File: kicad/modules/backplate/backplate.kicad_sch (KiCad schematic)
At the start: 1 part, among them J1 10018784-10210TLF

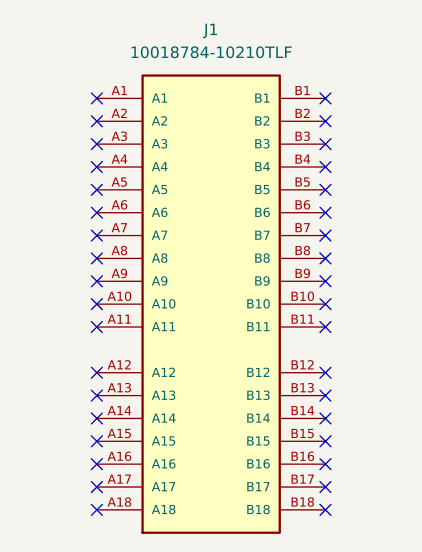
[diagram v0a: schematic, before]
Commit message: update PCIe nets
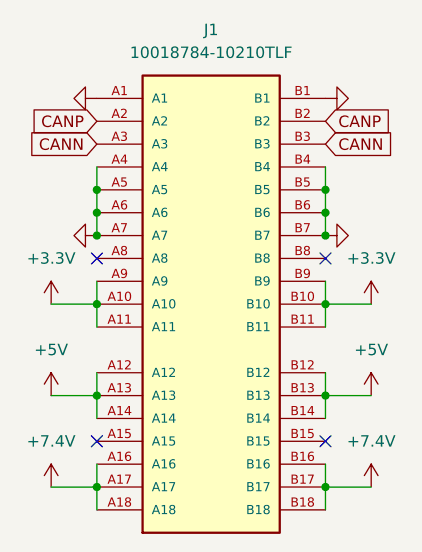
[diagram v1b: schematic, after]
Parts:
- J1: digikey # (none) -> 609-2029-ND; digikey link (none) -> https://www.digikey.ca/en/products/detail/amphenol-cs-fci/1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
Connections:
- net GND: now reaches J1.A1
- net GND: now also J1.A4, J1.A5, J1.A6, J1.A7, J1.B1, J1.B4, J1.B5, J1.B6, J1.B7
- net +3.3V: now reaches J1.A10
- net +3.3V: now also J1.A11, J1.A9, J1.B10, J1.B11, J1.B9
- net +5V: now reaches J1.A12
- net +5V: now also J1.A13, J1.A14, J1.B12, J1.B13, J1.B14
- net +7.4V: now reaches J1.A16
- net +7.4V: now also J1.A17, J1.A18, J1.B16, J1.B17, J1.B18
- net CANP: now reaches J1.A2
- net CANP: now also J1.B2
- net CANN: now reaches J1.A3
- net CANN: now also J1.B3
- no-connect marks 36 -> 4

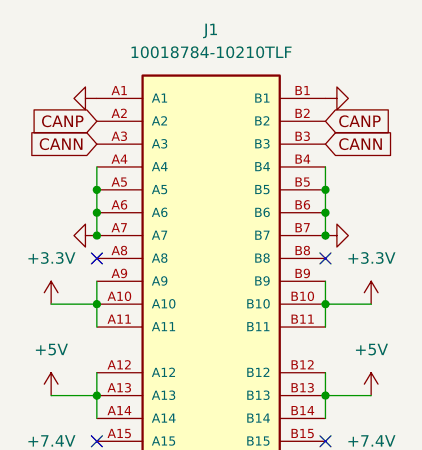
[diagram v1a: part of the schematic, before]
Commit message: backplate: update PCIe pins
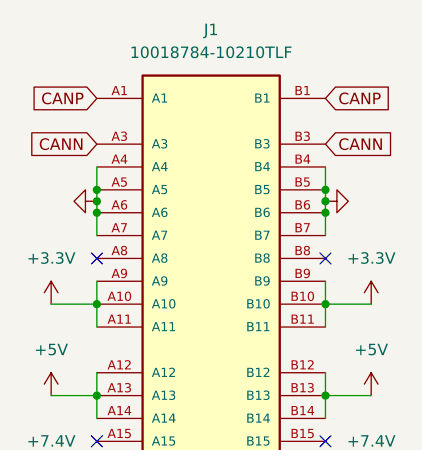
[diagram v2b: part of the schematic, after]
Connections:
- net CANP: now also J1.A1, J1.B1; no longer J1.A2, J1.B2
- net GND: no longer J1.A1, J1.B1
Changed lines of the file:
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@@
-	)
-	(junction
-		(at 140.97 81.28)
-		(diameter 0)
-		(color 0 0 0 0)
 	)
 	(junction
@@
 	)
 	(junction
+		(at 140.97 77.47)
+		(diameter 0)
+		(color 0 0 0 0)
+	)
+	(junction
 		(at 140.97 88.9)
 		(diameter 0)
@@
 	)
 	(junction
-		(at 115.57 81.28)
-		(diameter 0)
-		(color 0 0 0 0)
-	)
-	(junction
 		(at 115.57 78.74)
 		(diameter 0)
@@
 	)
 	(junction
+		(at 115.57 77.47)
+		(diameter 0)
+		(color 0 0 0 0)
+	)
+	(junction
 		(at 140.97 109.22)
 		(diameter 0)
@@
 	(wire
 		(pts
-			(xy 115.57 76.2) (xy 115.57 78.74)
+			(xy 115.57 76.2) (xy 115.57 77.47)
 		)
 		(stroke
@@
 	(wire
 		(pts
-			(xy 140.97 76.2) (xy 140.97 78.74)
+			(xy 140.97 76.2) (xy 140.97 77.47)
+		)
+		(stroke
+			(width 0)
+			(type default)
+		)
+	)
+	(wire
+		(pts
+			(xy 140.97 77.47) (xy 140.97 78.74)
 		)
 		(stroke
@@
 		(pts
 			(xy 146.05 109.22) (xy 140.97 109.22)
+		)
+		(stroke
+			(width 0)
+			(type default)
+		)
+	)
+	(wire
+		(pts
+			(xy 115.57 77.47) (xy 115.57 78.74)
 		)
 		(stroke
@@
 	(global_label "CANP"
 		(shape input)
-		(at 140.97 68.58 0)
+		(at 140.97 66.04 0)
 		(fields_autoplaced yes)
 		(effects
@@
 		)
 		(property "Intersheetrefs" "${INTERSHEET_REFS}"
-			(at 148.9143 68.58 0)
+			(at 148.9143 66.04 0)
 			(effects
 				(font
@@
 	(global_label "CANP"
 		(shape input)
-		(at 115.57 68.58 180)
+		(at 115.57 66.04 180)
 		(fields_autoplaced yes)
 		(effects
@@
 		)
 		(property "Intersheetrefs" "${INTERSHEET_REFS}"
-			(at 107.6257 68.58 0)
+			(at 107.6257 66.04 0)
 			(effects
 				(font
@@
 		(pin "A12"
 		)
-		(pin "A2"
-		)
 		(pin "B18"
-		)
-		(pin "B2"
 		)
 		(pin "A8"
@@
 	(symbol
 		(lib_id "power:GND")
-		(at 140.97 81.28 90)
+		(at 140.97 77.47 90)
 		(unit 1)
 		(exclude_from_sim no)
@@
 		(fields_autoplaced yes)
 		(property "Reference" "#PWR02"
-			(at 147.32 81.28 0)
+			(at 147.32 77.47 0)
 			(effects
 				(font
@@
 		)
 		(property "Value" "GND"
-			(at 146.05 81.28 0)
+			(at 146.05 77.47 0)
 			(effects
 				(font
@@
 		)
 		(property "Footprint" ""
-			(at 140.97 81.28 0)
+			(at 140.97 77.47 0)
 			(effects
 				(font
@@
 		)
 		(property "Datasheet" ""
-			(at 140.97 81.28 0)
+			(at 140.97 77.47 0)
 			(effects
 				(font
@@
 		)
 		(property "Description" "Power symbol creates a global label with name \"GND\" , ground"
-			(at 140.97 81.28 0)
+			(at 140.97 77.47 0)
 			(effects
 				(font
@@
 	(symbol
 		(lib_id "power:GND")
-		(at 140.97 66.04 90)
-		(unit 1)
-		(exclude_from_sim no)
-		(in_bom yes)
-		(on_board yes)
-		(dnp no)
-		(fields_autoplaced yes)
-		(property "Reference" "#PWR01"
-			(at 147.32 66.04 0)
-			(effects
-				(font
-					(size 1.27 1.27)
-				)
-				(hide yes)
-			)
-		)
-		(property "Value" "GND"
-			(at 144.78 66.0399 90)
-			(effects
-				(font
-					(size 1.27 1.27)
-				)
-				(justify right)
-				(hide yes)
-			)
-		)
-		(property "Footprint" ""
-			(at 140.97 66.04 0)
-			(effects
-				(font
-					(size 1.27 1.27)
-				)
-				(hide yes)
-			)
-		)
-		(property "Datasheet" ""
-			(at 140.97 66.04 0)
-			(effects
-				(font
-					(size 1.27 1.27)
-				)
-				(hide yes)
-			)
-		)
-		(property "Description" "Power symbol creates a global label with name \"GND\" , ground"
-			(at 140.97 66.04 0)
-			(effects
-				(font
-					(size 1.27 1.27)
-				)
-				(hide yes)
-			)
-		)
-		(pin "1"
-		)
-		(instances
-			(project "backplate"
-				(path "/3ac1a34a-3a2d-4f8e-be23-a5fa61208278"
-					(reference "#PWR01")
-					(unit 1)
-				)
-			)
-		)
-	)
-	(symbol
-		(lib_id "power:GND")
-		(at 115.57 81.28 270)
+		(at 115.57 77.47 270)
 		(mirror x)
 		(unit 1)
@@
 		(fields_autoplaced yes)
 		(property "Reference" "#PWR07"
-			(at 109.22 81.28 0)
+			(at 109.22 77.47 0)
 			(effects
 				(font
@@
 		)
 		(property "Value" "GND"
-			(at 110.49 81.28 0)
+			(at 110.49 77.47 0)
 			(effects
 				(font
@@
 		)
 		(property "Footprint" ""
-			(at 115.57 81.28 0)
+			(at 115.57 77.47 0)
 			(effects
 				(font
@@
 		)
 		(property "Datasheet" ""
-			(at 115.57 81.28 0)
+			(at 115.57 77.47 0)
 			(effects
 				(font
@@
 		)
 		(property "Description" "Power symbol creates a global label with name \"GND\" , ground"
-			(at 115.57 81.28 0)
+			(at 115.57 77.47 0)
 			(effects
 				(font
@@
 					(unit 1)
 				)
-			)
-		)
-	)
-	(symbol
-		(lib_id "power:GND")
-		(at 115.57 66.04 270)
-		(mirror x)
-		(unit 1)
-		(exclude_from_sim no)
-		(in_bom yes)
-		(on_board yes)
-		(dnp no)
-		(fields_autoplaced yes)
-		(property "Reference" "#PWR06"
-			(at 109.22 66.04 0)
-			(effects
-				(font
-					(size 1.27 1.27)
-				)
-				(hide yes)
-			)
-		)
-		(property "Value" "GND"
-			(at 111.76 66.0399 90)
-			(effects
-				(font
-					(size 1.27 1.27)
-				)
-				(justify right)
-				(hide yes)
-			)
-		)
-		(property "Footprint" ""
-			(at 115.57 66.04 0)
-			(effects
-				(font
-					(size 1.27 1.27)
-				)
-				(hide yes)
-			)
-		)
-		(property "Datasheet" ""
-			(at 115.57 66.04 0)
-			(effects
-				(font
-					(size 1.27 1.27)
-				)
-				(hide yes)
-			)
-		)
-		(property "Description" "Power symbol creates a global label with name \"GND\" , ground"
-			(at 115.57 66.04 0)
-			(effects
-				(font
-					(size 1.27 1.27)
-				)
-				(hide yes)
-			)
-		)
-		(pin "1"
-		)
-		(instances
-			(project "backplate"
-				(path "/3ac1a34a-3a2d-4f8e-be23-a5fa61208278"
-					(reference "#PWR06")
-					(unit 1)
-				)

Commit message: backplate: finish initial revision
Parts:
- added R1, R2: 120, Resistor_SMD:R_0805_2012Metric, symbol Device:R
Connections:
- net CANN: now also R1.2, R2.2; no longer J1.B3
- net CANP: now also R1.1, R2.1; no longer J1.B1
- net GND: now also J1.B1, J1.B3
